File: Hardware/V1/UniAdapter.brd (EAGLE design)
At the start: 55 x 20.9 mm, 19 parts, among them IC1 LD1117S33TR, U1 STM32F072CBT6, X1 CAN Bus

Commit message: UniAdapter 1.0 (PCB-POOL Order)
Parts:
- SB0: device rcl:R0603 -> jumper:SJ
- moved C4 0.76 mm to (27.4, 18.6)
- moved SB0 0.28 mm to (30.5, 18.5)
- moved R2 0.13 mm to (33.6, 18.7)
- moved C3 0.07 mm to (33.6, 15.2)
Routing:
- net VCC: track 75.1 -> 74.5 mm
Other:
- board size 55 x 20.9 mm -> 40 x 20.9 mm
- board text added: "(RX)"
- board text added: "+"
- board text added: "PORT1"
- board text added: "PORT2"
- board text added: "S"
- board text added: "UniAdapter 1.0"
- board text added: "_"
- board text added: "cemizm"
- board text removed: "10 mm"

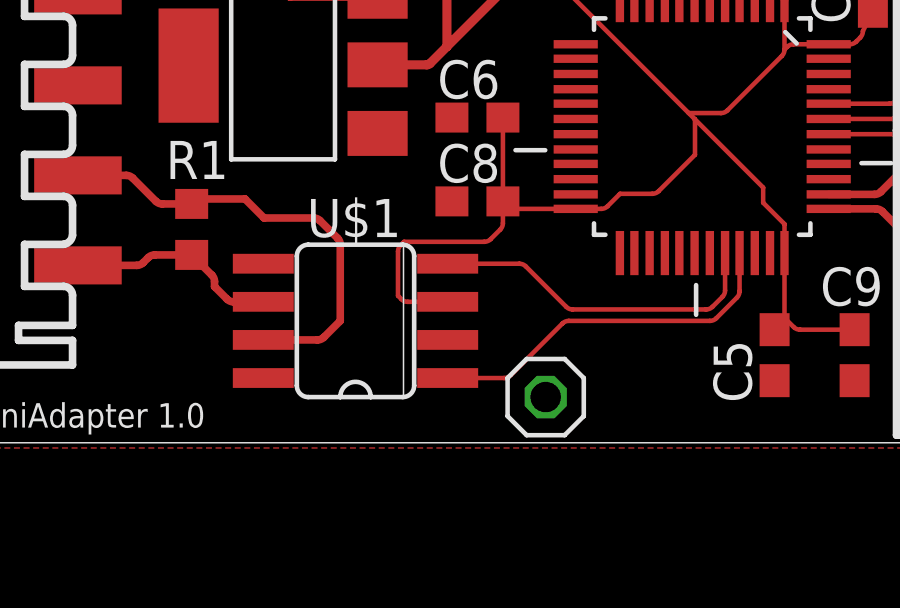
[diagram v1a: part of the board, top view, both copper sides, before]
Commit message: Replace HVD230 <-> HVD232
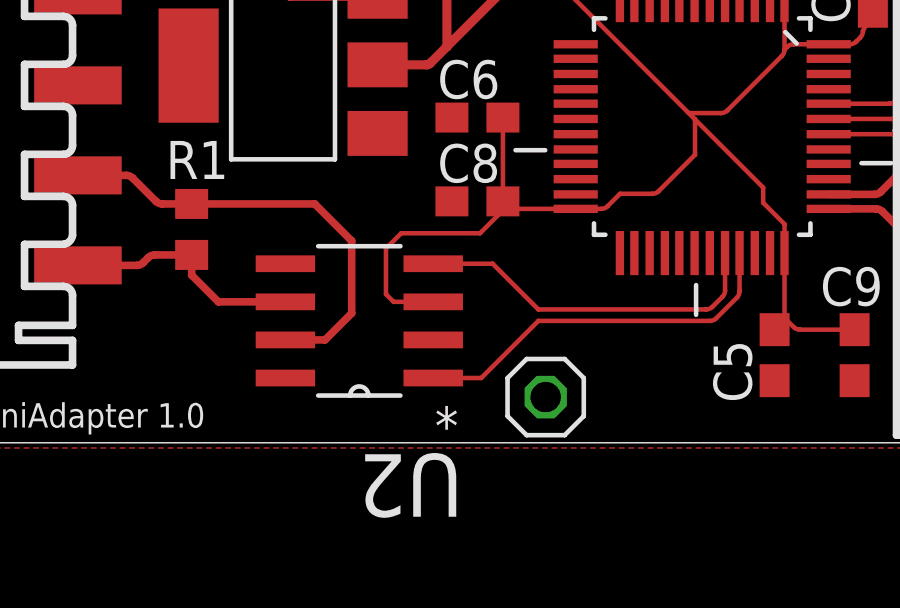
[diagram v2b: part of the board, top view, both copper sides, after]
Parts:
- removed U$1: SN65HVD230D/231D_S08, can:SO08
- added U2: SN65HVD232D, texas:SOIC127P600X175-8N
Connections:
- net CANRX: now also U2.4; no longer U$1.4
- net CANTX: now also U2.1; no longer U$1.1
- net CAN_H: now also U2.7; no longer U$1.7
- net CAN_L: now also U2.6; no longer U$1.6
- net GND: now also U2.2; no longer U$1.2
- net VCC: now also U2.3; no longer U$1.3
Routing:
- net CAN_L: track 7.06 -> 8.06 mm
- net CANTX: track 12.2 -> 12.7 mm
- net CANRX: track 11.4 -> 11.9 mm

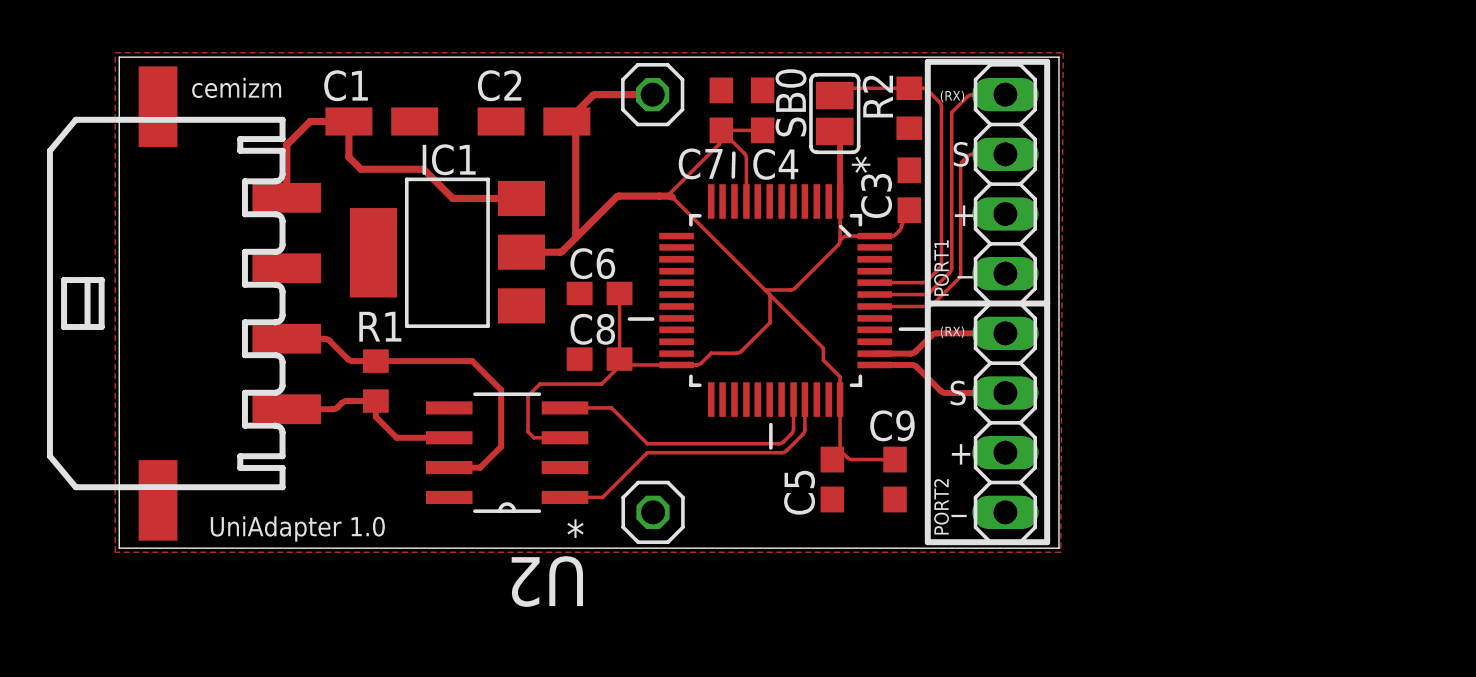
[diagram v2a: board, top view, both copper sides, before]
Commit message: Bestückungsdruck angepasst
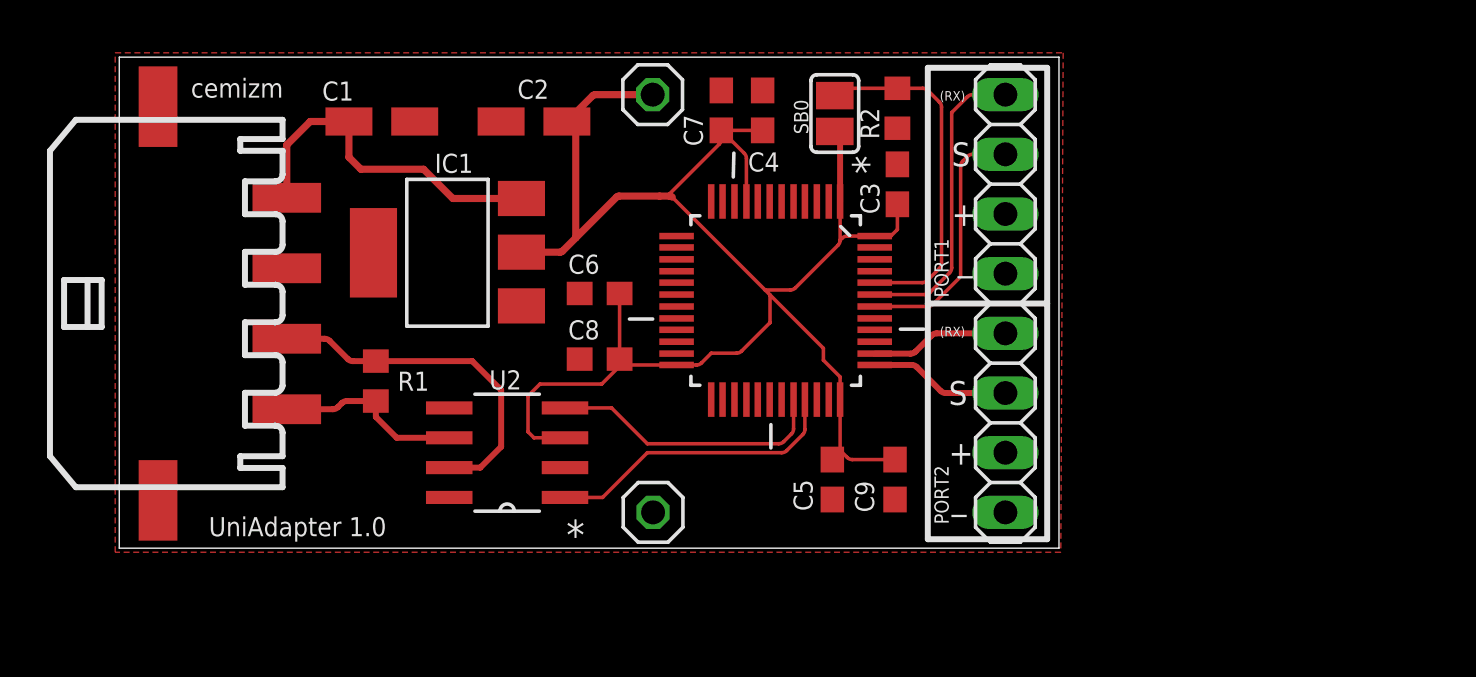
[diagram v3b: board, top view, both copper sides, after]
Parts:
- moved C3 0.57 mm to (33.1, 15.5)
- moved R2 0.51 mm to (33.1, 18.7)

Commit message: [HW] UniAdapter 1.1
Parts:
- removed JP1: (no value), pinhead:1X08
- removed JP2, JP3: (no value), pinhead:1X01
- removed SB0: (no value), jumper:SJ
- removed U1: STM32F072CBT6, STM32F0:QFP50P900X900X160-48N
- removed U2: SN65HVD232D, texas:SOIC127P600X175-8N
- added EXTENS.: SM05B-SRSS-TB, con-jst2:SM05B-SRSS-TB
- added IC2: SN65HVD232D, texas:SOIC127P600X175-8N
- added IC3: STM32F072CBT6, STM32F0:LQFP48
- added LED_GREEN, LED_RED: (no value), led:CHIPLED_0603
- added PORT1, PORT2: SM03B-SRSS-TB, con-jst2:SM03B-SRSS-TB
- added R3: 1.8K, rcl:R0603
- added R4, R5: 55Ohm, rcl:R0603
- added X2: CAN Bus, con-molex-micro-fit-3_0:43650-0412
- C4: value 10nF -> 100nF
- C6: value 100nF -> 10nF
- R1: value 120 Ohm -> 10k
- R2: value 10k -> 1.8K
- moved C4 24.0 mm to (9.86, 2.29), turned to 270 degrees
- moved C1 17.5 mm to (4.50, 2.00)
- moved C9 14.7 mm to (18.4, 1.27), turned to 180 degrees
- moved R1 14.6 mm to (21.5, 17.1)
- moved C2 14.5 mm to (4.98, 11.2), turned to 0 degrees
- moved R2 13.5 mm to (19.7, 17.1)
- moved C3 13.3 mm to (20.2, 12.6)
- moved C7 11.4 mm to (14.4, 17.1)
- moved IC1 10.7 mm to (5.08, 6.60), turned to 270 degrees
- moved C8 10.3 mm to (11.9, 2.29), turned to 270 degrees
- moved C5 9.40 mm to (21.0, 2.16), turned to 90 degrees
- moved C6 7.64 mm to (16.1, 17.1), turned to 90 degrees
- moved X1 3.35 mm to (5.00, 10.5), flipped to the bottom, turned to 90 degrees
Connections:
- removed net NC1: JP1.3
- removed net NC2: JP1.7
- new net I2C1_SCL: EXTENS..2, IC3.45, R2.2
- new net I2C1_SDA: EXTENS..1, IC3.46, R3.2
- new net LD_GREEN: IC3.11, R5.1
- new net LD_RED: IC3.10, R4.1
- new net N$3: LED_RED.A, R4.2
- new net N$4: LED_GREEN.A, R5.2
- net 6V: now also X2.P$4
- net BOOT0: now also EXTENS..3, IC3.44, R1.1; no longer R2.1, SB0.1, U1.44
- net CANRX: now also IC2.4, IC3.32; no longer U1.32, U2.4
- net CANTX: now also IC2.1, IC3.33; no longer U1.33, U2.1
- net CAN_H: now also IC2.7, X2.P$2; no longer R1.2, U2.7
- net CAN_L: now also IC2.6, X2.P$1; no longer R1.1, U2.6
- net GND: now also EXTENS..5, IC2.2, IC3.23, IC3.35, IC3.47, IC3.8, LED_GREEN.C, LED_RED.C, PORT1.3, PORT2.3, R1.2, X2.P$3; no longer JP1.4, JP1.8, JP3.1, R2.2, U1.23, U1.35, U1.47, U1.8, U2.2
- net USART1RX: now also IC3.43, PORT1.2; no longer JP1.1, U1.43
- net USART1TX: now also IC3.42, PORT1.1; no longer JP1.2, U1.42
- net USART2RX: now also IC3.38, PORT2.2; no longer JP1.5, U1.38
- net USART2TX: now also IC3.37, PORT2.1; no longer JP1.6, U1.37
- net VCC: now also EXTENS..4, IC2.3, IC3.1, IC3.24, IC3.36, IC3.48, IC3.9, R2.1, R3.1; no longer JP2.1, SB0.2, U1.1, U1.24, U1.36, U1.48, U1.9, U2.3
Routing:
- net CAN_L: track 8.06 -> 41.6 mm, vias 0 -> 1
- net VCC: track 74.3 -> 46.1 mm, vias 0 -> 8
- net CAN_H: track 15.0 -> 40.2 mm, vias 0 -> 1
- net CANRX: track 11.9 -> 32.9 mm, vias 0 -> 2
- net I2C1_SCL: track 0.00 -> 18.5 mm
- net I2C1_SDA: track 0.00 -> 15.4 mm
- net GND: track 0.00 -> 14.1 mm, vias 0 -> 2
- net 6V: track 14.9 -> 28.4 mm, vias 0 -> 3
- net CANTX: track 12.7 -> 25.2 mm, vias 0 -> 2
- net N$3: track 0.00 -> 8.86 mm
- net USART1RX: track 13.0 -> 5.12 mm
- net LD_GREEN: track 0.00 -> 6.87 mm
- net USART1TX: track 11.0 -> 4.92 mm
- net N$4: track 0.00 -> 5.95 mm
- net LD_RED: track 0.00 -> 5.52 mm
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- added copper zone on layer 16, net VCC
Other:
- board size 40 x 20.9 mm -> 30 x 21 mm
- board text added: "UniAdapter 1.1"
- board text removed: "(RX)"
- board text removed: "+"
- board text removed: "PORT1"
- board text removed: "PORT2"
- board text removed: "S"
- board text removed: "UniAdapter 1.0"
- board text removed: "_"

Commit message: Leds added
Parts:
- LD1: value (none) -> RED
- LD2: value (none) -> GREEN
- renumbered LED_GREEN to LD2, LED_RED to LD1
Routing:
- net CAN_H: track 40.2 -> 32.8 mm
- net CAN_L: track 41.6 -> 36.3 mm
- net VCC: track 46.1 -> 45.5 mm
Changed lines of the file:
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@@
 <attribute name="VALUE" x="12.7" y="16.51" size="1.27" layer="27" rot="R90"/>
 </element>
-<element name="LED_RED" library="led" package="CHIPLED_0603" value="" x="9.398" y="12.573" smashed="yes" rot="R180">
+<element name="LD1" library="led" package="CHIPLED_0603" value="RED" x="9.398" y="12.573" smashed="yes" rot="R180">
 <attribute name="VALUE" x="7.493" y="13.843" size="1.27" layer="27" rot="R270"/>
 </element>
-<element name="LED_GREEN" library="led" package="CHIPLED_0603" value="" x="11.049" y="12.573" smashed="yes" rot="R180">
+<element name="LD2" library="led" package="CHIPLED_0603" value="GREEN" x="11.049" y="12.573" smashed="yes" rot="R180">
 <attribute name="VALUE" x="9.144" y="13.843" size="1.27" layer="27" rot="R270"/>
 </element>
@@
 <wire x1="9.8806" y1="4.2926" x2="9.906" y2="3.055" width="0.254" layer="1"/>
 <wire x1="9.906" y1="3.055" x2="9.86" y2="3.136" width="0.254" layer="1"/>
-<wire x1="21.59" y1="1.27" x2="21.717" y2="1.27" width="0.254" layer="16"/>
 <wire x1="24.711" y1="17.635" x2="24.729" y2="17.653" width="0.254" layer="1"/>
 <wire x1="24.729" y1="17.653" x2="27.305" y2="17.653" width="0.254" layer="1"/>
@@
 <contactref element="R2" pad="1"/>
 <wire x1="4.572" y1="7.366" x2="4.572" y2="9.8" width="0.6096" layer="1"/>
-<wire x1="5.715" y1="9.017" x2="5.207" y2="9.144" width="0.6096" layer="16"/>
 <wire x1="3.577" y1="11.176" x2="3.577" y2="10.795" width="0.6096" layer="1"/>
 <wire x1="3.577" y1="10.795" x2="4.572" y2="9.8" width="0.6096" layer="1"/>
@@
 <wire x1="17.653" y1="16.764" x2="21.717" y2="16.764" width="0.4064" layer="16"/>
 <wire x1="21.717" y1="16.764" x2="23.114" y2="15.367" width="0.4064" layer="16"/>
-<wire x1="23.114" y1="15.367" x2="23.114" y2="12.573" width="0.4064" layer="16"/>
-<wire x1="23.114" y1="12.573" x2="23.876" y2="11.811" width="0.4064" layer="16"/>
-<wire x1="23.876" y1="11.811" x2="25.4" y2="11.811" width="0.4064" layer="16"/>
-<wire x1="25.4" y1="11.811" x2="27.051" y2="10.16" width="0.4064" layer="16"/>
-<wire x1="27.051" y1="10.16" x2="27.051" y2="8.763" width="0.4064" layer="16"/>
-<wire x1="27.051" y1="8.763" x2="24.288" y2="6" width="0.4064" layer="16"/>
-<wire x1="24.288" y1="6" x2="19.52" y2="6" width="0.4064" layer="16"/>
+<wire x1="22.352" y1="6" x2="19.52" y2="6" width="0.4064" layer="16"/>
+<wire x1="23.114" y1="15.367" x2="23.114" y2="6.762" width="0.4064" layer="16"/>
+<wire x1="23.114" y1="6.762" x2="22.352" y2="6" width="0.4064" layer="16"/>
 </signal>
 <signal name="CAN_H">
@@
 <wire x1="17.907" y1="16.129" x2="21.463" y2="16.129" width="0.4064" layer="16"/>
 <wire x1="21.463" y1="16.129" x2="22.479" y2="15.113" width="0.4064" layer="16"/>
-<wire x1="22.479" y1="15.113" x2="22.479" y2="12.319" width="0.4064" layer="16"/>
-<wire x1="22.479" y1="12.319" x2="23.622" y2="11.176" width="0.4064" layer="16"/>
-<wire x1="23.622" y1="11.176" x2="25.146" y2="11.176" width="0.4064" layer="16"/>
-<wire x1="25.146" y1="11.176" x2="26.416" y2="9.906" width="0.4064" layer="16"/>
-<wire x1="26.416" y1="9.906" x2="26.416" y2="9.017" width="0.4064" layer="16"/>
-<wire x1="26.416" y1="9.017" x2="25.781" y2="8.382" width="0.4064" layer="16"/>
-<wire x1="25.781" y1="8.382" x2="24.892" y2="8.382" width="0.4064" layer="16"/>
-<wire x1="24.892" y1="8.382" x2="24.274" y2="9" width="0.4064" layer="16"/>
-<wire x1="24.274" y1="9" x2="19.52" y2="9" width="0.4064" layer="16"/>
+<wire x1="22.479" y1="15.113" x2="22.479" y2="9.889" width="0.4064" layer="16"/>
+<wire x1="21.59" y1="9" x2="19.52" y2="9" width="0.4064" layer="16"/>
+<wire x1="22.479" y1="9.889" x2="21.59" y2="9" width="0.4064" layer="16"/>
 </signal>
 <signal name="GND">
@@
 <via x="16.129" y="9.271" extent="1-16" drill="0.3048"/>
 <wire x1="16.637" y1="9.779" x2="16.129" y2="9.271" width="0.6096" layer="16"/>
-<contactref element="LED_GREEN" pad="C"/>
-<contactref element="LED_RED" pad="C"/>
+<contactref element="LD2" pad="C"/>
+<contactref element="LD1" pad="C"/>
 </signal>
 <signal name="USART2TX">
@@
 <signal name="N$3">
 <contactref element="R4" pad="2"/>
-<contactref element="LED_RED" pad="A"/>
+<contactref element="LD1" pad="A"/>
 <wire x1="12.573" y1="17.995" x2="11.645" y2="18.923" width="0.254" layer="1"/>
 <wire x1="11.645" y1="18.923" x2="9.906" y2="18.923" width="0.254" layer="1"/>
@@
 </signal>
 <signal name="N$4">
-<contactref element="LED_GREEN" pad="A"/>
+<contactref element="LD2" pad="A"/>
 <contactref element="R5" pad="2"/>
 <wire x1="10.795" y1="17.995" x2="9.994" y2="17.995" width="0.254" layer="1"/>

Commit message: Revert "Revert "AnySense 1.1""
This reverts commit 477dbe3a037d16c593f52677c37ec78f086be774.
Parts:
- R4: value 55Ohm -> 68Ohm
- R5: value 55Ohm -> 56Ohm
- moved C5 0.76 mm to (20.2, 2.16)
- moved C9 0.63 mm to (17.8, 1.27)
- moved C3 0.13 mm to (20.3, 12.6)
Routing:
- net VCC: track 45.5 -> 42.2 mm
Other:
- board text added: "AnySense 1.1"
- board text removed: "UniAdapter 1.1"
- board text removed: "cemizm"
